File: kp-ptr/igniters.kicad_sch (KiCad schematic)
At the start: 40 parts

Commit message: Footprints IN IMU9DOF OUT Signed-off-by: kretu <krecik@gmail.com>
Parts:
- C39, C40, C41, C42: renamed from C?; footprint (none) -> Capacitor_SMD:C_01005_0402Metric_Pad0.57x0.30mm_HandSolder
- F1, F2, F3, F4: renamed from F?; footprint (none) -> Fuse:Fuse_1206_3216Metric_Pad1.42x1.75mm_HandSolder
- J6, J7, J8, J9: renamed from J?; footprint (none) -> TerminalBlock_TE-Connectivity:TerminalBlock_TE_282834-2_1x02_P2.54mm_Horizontal
- R41, R42, R43, R44, R45, R46, R47, R48, R49, R50, R51, R52, R53, R54, R55, R56, R57, R58, R59, R60: renamed from R?; footprint (none) -> Resistor_SMD:R_01005_0402Metric_Pad0.57x0.30mm_HandSolder
- gave numbers to parts that had none: 8

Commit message: Footprinty drobnicy
Signed-off-by: kretu <krecik@gmail.com>
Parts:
- C39, C40, C41, C42: footprint Capacitor_SMD:C_01005_0402Metric_Pad0.57x0.30mm_HandSolder -> Capacitor_SMD:C_0402_1005Metric_Pad0.74x0.62mm_HandSolder
- R41, R42, R43, R44, R45, R46, R47, R48, R49, R50, R51, R52, R53, R54, R55, R56, R57, R58, R59, R60: footprint Resistor_SMD:R_01005_0402Metric_Pad0.57x0.30mm_HandSolder -> Resistor_SMD:R_0402_1005Metric_Pad0.72x0.64mm_HandSolder
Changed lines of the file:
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@@
     (property "Reference" "R41" (id 0) (at 62.23 100.33 90))
     (property "Value" "10k" (id 1) (at 57.15 100.33 90))
-    (property "Footprint" "Resistor_SMD:R_01005_0402Metric_Pad0.57x0.30mm_HandSolder" (id 2) (at 57.912 99.06 90)
+    (property "Footprint" "Resistor_SMD:R_0402_1005Metric_Pad0.72x0.64mm_HandSolder" (id 2) (at 57.912 99.06 90)
       (effects (font (size 1.27 1.27)) hide)
     )
@@
     (property "Reference" "R52" (id 0) (at 144.78 149.86 90))
     (property "Value" "10k" (id 1) (at 139.7 149.86 90))
-    (property "Footprint" "Resistor_SMD:R_01005_0402Metric_Pad0.57x0.30mm_HandSolder" (id 2) (at 140.462 148.59 90)
+    (property "Footprint" "Resistor_SMD:R_0402_1005Metric_Pad0.72x0.64mm_HandSolder" (id 2) (at 140.462 148.59 90)
       (effects (font (size 1.27 1.27)) hide)
     )
@@
     (property "Reference" "R58" (id 0) (at 151.13 121.92 90))
     (property "Value" "10k" (id 1) (at 151.13 116.84 90))
-    (property "Footprint" "Resistor_SMD:R_01005_0402Metric_Pad0.57x0.30mm_HandSolder" (id 2) (at 151.892 120.65 90)
+    (property "Footprint" "Resistor_SMD:R_0402_1005Metric_Pad0.72x0.64mm_HandSolder" (id 2) (at 151.892 120.65 90)
       (effects (font (size 1.27 1.27)) hide)
     )
@@
       (effects (font (size 1.27 1.27)) (justify left))
     )
-    (property "Footprint" "Capacitor_SMD:C_01005_0402Metric_Pad0.57x0.30mm_HandSolder" (id 2) (at 158.4452 124.46 0)
+    (property "Footprint" "Capacitor_SMD:C_0402_1005Metric_Pad0.74x0.62mm_HandSolder" (id 2) (at 158.4452 124.46 0)
       (effects (font (size 1.27 1.27)) hide)
     )
@@
     (property "Reference" "R54" (id 0) (at 148.59 134.62 90))
     (property "Value" "10k" (id 1) (at 143.51 134.62 90))
-    (property "Footprint" "Resistor_SMD:R_01005_0402Metric_Pad0.57x0.30mm_HandSolder" (id 2) (at 144.272 133.35 90)
+    (property "Footprint" "Resistor_SMD:R_0402_1005Metric_Pad0.72x0.64mm_HandSolder" (id 2) (at 144.272 133.35 90)
       (effects (font (size 1.27 1.27)) hide)
     )
@@
     (property "Reference" "R60" (id 0) (at 189.23 127 90))
     (property "Value" "10k" (id 1) (at 189.23 121.92 90))
-    (property "Footprint" "Resistor_SMD:R_01005_0402Metric_Pad0.57x0.30mm_HandSolder" (id 2) (at 189.992 125.73 90)
+    (property "Footprint" "Resistor_SMD:R_0402_1005Metric_Pad0.72x0.64mm_HandSolder" (id 2) (at 189.992 125.73 90)
       (effects (font (size 1.27 1.27)) hide)
     )
@@
     (property "Reference" "R46" (id 0) (at 67.31 143.51 90))
     (property "Value" "100k" (id 1) (at 67.31 148.59 90))
-    (property "Footprint" "Resistor_SMD:R_01005_0402Metric_Pad0.57x0.30mm_HandSolder" (id 2) (at 66.04 147.828 90)
+    (property "Footprint" "Resistor_SMD:R_0402_1005Metric_Pad0.72x0.64mm_HandSolder" (id 2) (at 66.04 147.828 90)
       (effects (font (size 1.27 1.27)) hide)
     )
@@
     (property "Reference" "R57" (id 0) (at 151.13 72.39 90))
     (property "Value" "10k" (id 1) (at 151.13 67.31 90))
-    (property "Footprint" "Resistor_SMD:R_01005_0402Metric_Pad0.57x0.30mm_HandSolder" (id 2) (at 151.892 71.12 90)
+    (property "Footprint" "Resistor_SMD:R_0402_1005Metric_Pad0.72x0.64mm_HandSolder" (id 2) (at 151.892 71.12 90)
       (effects (font (size 1.27 1.27)) hide)
     )
@@
     (property "Reference" "R47" (id 0) (at 68.58 72.39 90))
     (property "Value" "10k" (id 1) (at 68.58 67.31 90))
-    (property "Footprint" "Resistor_SMD:R_01005_0402Metric_Pad0.57x0.30mm_HandSolder" (id 2) (at 69.342 71.12 90)
+    (property "Footprint" "Resistor_SMD:R_0402_1005Metric_Pad0.72x0.64mm_HandSolder" (id 2) (at 69.342 71.12 90)
       (effects (font (size 1.27 1.27)) hide)
     )
@@
     (property "Reference" "R50" (id 0) (at 106.68 128.27 90))
     (property "Value" "10k" (id 1) (at 106.68 123.19 90))
-    (property "Footprint" "Resistor_SMD:R_01005_0402Metric_Pad0.57x0.30mm_HandSolder" (id 2) (at 107.442 127 90)
+    (property "Footprint" "Resistor_SMD:R_0402_1005Metric_Pad0.72x0.64mm_HandSolder" (id 2) (at 107.442 127 90)
       (effects (font (size 1.27 1.27)) hide)
     )
@@
     (property "Reference" "R42" (id 0) (at 62.23 151.13 90))
     (property "Value" "10k" (id 1) (at 57.15 151.13 90))
-    (property "Footprint" "Resistor_SMD:R_01005_0402Metric_Pad0.57x0.30mm_HandSolder" (id 2) (at 57.912 149.86 90)
+    (property "Footprint" "Resistor_SMD:R_0402_1005Metric_Pad0.72x0.64mm_HandSolder" (id 2) (at 57.912 149.86 90)
       (effects (font (size 1.27 1.27)) hide)
     )
@@
     (property "Reference" "R59" (id 0) (at 189.23 77.47 90))
     (property "Value" "10k" (id 1) (at 189.23 72.39 90))
-    (property "Footprint" "Resistor_SMD:R_01005_0402Metric_Pad0.57x0.30mm_HandSolder" (id 2) (at 189.992 76.2 90)
+    (property "Footprint" "Resistor_SMD:R_0402_1005Metric_Pad0.72x0.64mm_HandSolder" (id 2) (at 189.992 76.2 90)
       (effects (font (size 1.27 1.27)) hide)
     )
@@
       (effects (font (size 1.27 1.27)) (justify left))
     )
-    (property "Footprint" "Capacitor_SMD:C_01005_0402Metric_Pad0.57x0.30mm_HandSolder" (id 2) (at 158.4452 74.93 0)
+    (property "Footprint" "Capacitor_SMD:C_0402_1005Metric_Pad0.74x0.62mm_HandSolder" (id 2) (at 158.4452 74.93 0)
       (effects (font (size 1.27 1.27)) hide)
     )
@@
     (property "Reference" "R51" (id 0) (at 144.78 100.33 90))
     (property "Value" "10k" (id 1) (at 139.7 100.33 90))
-    (property "Footprint" "Resistor_SMD:R_01005_0402Metric_Pad0.57x0.30mm_HandSolder" (id 2) (at 140.462 99.06 90)
+    (property "Footprint" "Resistor_SMD:R_0402_1005Metric_Pad0.72x0.64mm_HandSolder" (id 2) (at 140.462 99.06 90)
       (effects (font (size 1.27 1.27)) hide)
     )
@@
       (effects (font (size 1.27 1.27)) (justify left))
     )
-    (property "Footprint" "Capacitor_SMD:C_01005_0402Metric_Pad0.57x0.30mm_HandSolder" (id 2) (at 75.8952 74.93 0)
+    (property "Footprint" "Capacitor_SMD:C_0402_1005Metric_Pad0.74x0.62mm_HandSolder" (id 2) (at 75.8952 74.93 0)
       (effects (font (size 1.27 1.27)) hide)
     )
@@
     (property "Reference" "R48" (id 0) (at 68.58 123.19 90))
     (property "Value" "10k" (id 1) (at 68.58 118.11 90))
-    (property "Footprint" "Resistor_SMD:R_01005_0402Metric_Pad0.57x0.30mm_HandSolder" (id 2) (at 69.342 121.92 90)
+    (property "Footprint" "Resistor_SMD:R_0402_1005Metric_Pad0.72x0.64mm_HandSolder" (id 2) (at 69.342 121.92 90)
       (effects (font (size 1.27 1.27)) hide)
     )
@@
     (property "Reference" "R43" (id 0) (at 66.04 85.09 90))
     (property "Value" "10k" (id 1) (at 60.96 85.09 90))
-    (property "Footprint" "Resistor_SMD:R_01005_0402Metric_Pad0.57x0.30mm_HandSolder" (id 2) (at 61.722 83.82 90)
+    (property "Footprint" "Resistor_SMD:R_0402_1005Metric_Pad0.72x0.64mm_HandSolder" (id 2) (at 61.722 83.82 90)
       (effects (font (size 1.27 1.27)) hide)
     )
@@
     (property "Reference" "R55" (id 0) (at 149.86 92.71 90))
     (property "Value" "100k" (id 1) (at 149.86 97.79 90))
-    (property "Footprint" "Resistor_SMD:R_01005_0402Metric_Pad0.57x0.30mm_HandSolder" (id 2) (at 148.59 97.028 90)
+    (property "Footprint" "Resistor_SMD:R_0402_1005Metric_Pad0.72x0.64mm_HandSolder" (id 2) (at 148.59 97.028 90)
       (effects (font (size 1.27 1.27)) hide)
     )
@@
     (property "Reference" "R44" (id 0) (at 66.04 135.89 90))
     (property "Value" "10k" (id 1) (at 60.96 135.89 90))
-    (property "Footprint" "Resistor_SMD:R_01005_0402Metric_Pad0.57x0.30mm_HandSolder" (id 2) (at 61.722 134.62 90)
+    (property "Footprint" "Resistor_SMD:R_0402_1005Metric_Pad0.72x0.64mm_HandSolder" (id 2) (at 61.722 134.62 90)
       (effects (font (size 1.27 1.27)) hide)
     )
@@
       (effects (font (size 1.27 1.27)) (justify left))
     )
-    (property "Footprint" "Capacitor_SMD:C_01005_0402Metric_Pad0.57x0.30mm_HandSolder" (id 2) (at 75.8952 125.73 0)
+    (property "Footprint" "Capacitor_SMD:C_0402_1005Metric_Pad0.74x0.62mm_HandSolder" (id 2) (at 75.8952 125.73 0)
       (effects (font (size 1.27 1.27)) hide)
     )
@@
     (property "Reference" "R45" (id 0) (at 67.31 92.71 90))
     (property "Value" "100k" (id 1) (at 67.31 97.79 90))
-    (property "Footprint" "Resistor_SMD:R_01005_0402Metric_Pad0.57x0.30mm_HandSolder" (id 2) (at 66.04 97.028 90)
+    (property "Footprint" "Resistor_SMD:R_0402_1005Metric_Pad0.72x0.64mm_HandSolder" (id 2) (at 66.04 97.028 90)
       (effects (font (size 1.27 1.27)) hide)
     )
@@
     (property "Reference" "R56" (id 0) (at 149.86 142.24 90))
     (property "Value" "100k" (id 1) (at 149.86 147.32 90))
-    (property "Footprint" "Resistor_SMD:R_01005_0402Metric_Pad0.57x0.30mm_HandSolder" (id 2) (at 148.59 146.558 90)
+    (property "Footprint" "Resistor_SMD:R_0402_1005Metric_Pad0.72x0.64mm_HandSolder" (id 2) (at 148.59 146.558 90)
       (effects (font (size 1.27 1.27)) hide)
     )
@@
     (property "Reference" "R53" (id 0) (at 148.59 85.09 90))
     (property "Value" "10k" (id 1) (at 143.51 85.09 90))
-    (property "Footprint" "Resistor_SMD:R_01005_0402Metric_Pad0.57x0.30mm_HandSolder" (id 2) (at 144.272 83.82 90)
+    (property "Footprint" "Resistor_SMD:R_0402_1005Metric_Pad0.72x0.64mm_HandSolder" (id 2) (at 144.272 83.82 90)
       (effects (font (size 1.27 1.27)) hide)
     )
@@
     (property "Reference" "R49" (id 0) (at 106.68 77.47 90))
     (property "Value" "10k" (id 1) (at 106.68 72.39 90))
-    (property "Footprint" "Resistor_SMD:R_01005_0402Metric_Pad0.57x0.30mm_HandSolder" (id 2) (at 107.442 76.2 90)
-      (effects (font (size 1.27 1.27)) hide)
-    )
+    (property "Footprint" "Resistor_SMD:R_0402_1005Metric_Pad0.72x0.64mm_HandSolder" (id 2) (at 107.442 76.2 90)
+      (effects (font (size 1.27 1.27)) hide)
+    )

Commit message: Kilka zmian.
-dodany tranzystor P/N mosfet do biblioteki i zapalników
-dodany komentarz o impedancji ścieżek RF
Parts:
- removed Q10, Q11, Q6, Q7: NMOS_SOT23, Package_TO_SOT_SMD:SOT-23, symbol Transistor_FET:IRLML2060
- removed Q12, Q13, Q8, Q9: PMOS_SOT23, Package_TO_SOT_SMD:SOT-23, symbol Transistor_FET:IRLML6401
- added Q? (x8): DMC2025UFDB, symbol KP-PTR_lib:DMC2025UFDB
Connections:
- net Earth: now also Q?.S1, Q?.S1, Q?.S1, Q?.S1
- net IGN1_EN: now also Q?.G1 (G2)
- net IGN2_EN: now also Q?.G1 (G2)
- net IGN3_EN: now also Q?.G1 (G2)
- net IGN4_EN: now also Q?.G1 (G2)
- net at C41.2, R57.2: now also Q?.D1 (D2), Q?.G2
- net at C41.1, F3.2, R57.1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: now also Q?.S2
- net at J8.1 (Pin_1), R55.2, R59.2: now also Q?.D2
- net at C39.2, R47.2: now also Q?.D1 (D2), Q?.G2
- net at C39.1, F1.2, R47.1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: now also Q?.S2
- net at J6.1 (Pin_1), R45.2, R49.2: now also Q?.D2
- net at C42.2, R58.2: now also Q?.D1 (D2), Q?.G2
- net at J9.1 (Pin_1), R56.2, R60.2: now also Q?.D2
- net at C42.1, F4.2, R58.1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: now also Q?.S2
- net at J7.1 (Pin_1), R46.2, R50.2: now also Q?.D2
- net at C40.1, F2.2, R48.1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: now also Q?.S2
- net at C40.2, R48.2: now also Q?.D1 (D2), Q?.G2
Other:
- note removed: "Do dopracowania: -estetyka -zweryfikować z poprzednimi projektami"

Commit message: Update po spotkaniu
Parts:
- C39, C40, C41, C42: footprint Capacitor_SMD:C_0402_1005Metric_Pad0.74x0.62mm_HandSolder -> Capacitor_SMD:C_0402_1005Metric
- F1, F2, F3, F4: footprint Fuse:Fuse_1206_3216Metric_Pad1.42x1.75mm_HandSolder -> Fuse:Fuse_0805_2012Metric
- R41, R42, R43, R44, R45, R46, R47, R48, R49, R50, R51, R52, R53, R54, R55, R56, R57, R58, R59, R60: footprint Resistor_SMD:R_0402_1005Metric_Pad0.72x0.64mm_HandSolder -> Resistor_SMD:R_0402_1005Metric
- gave numbers to parts that had none: 4

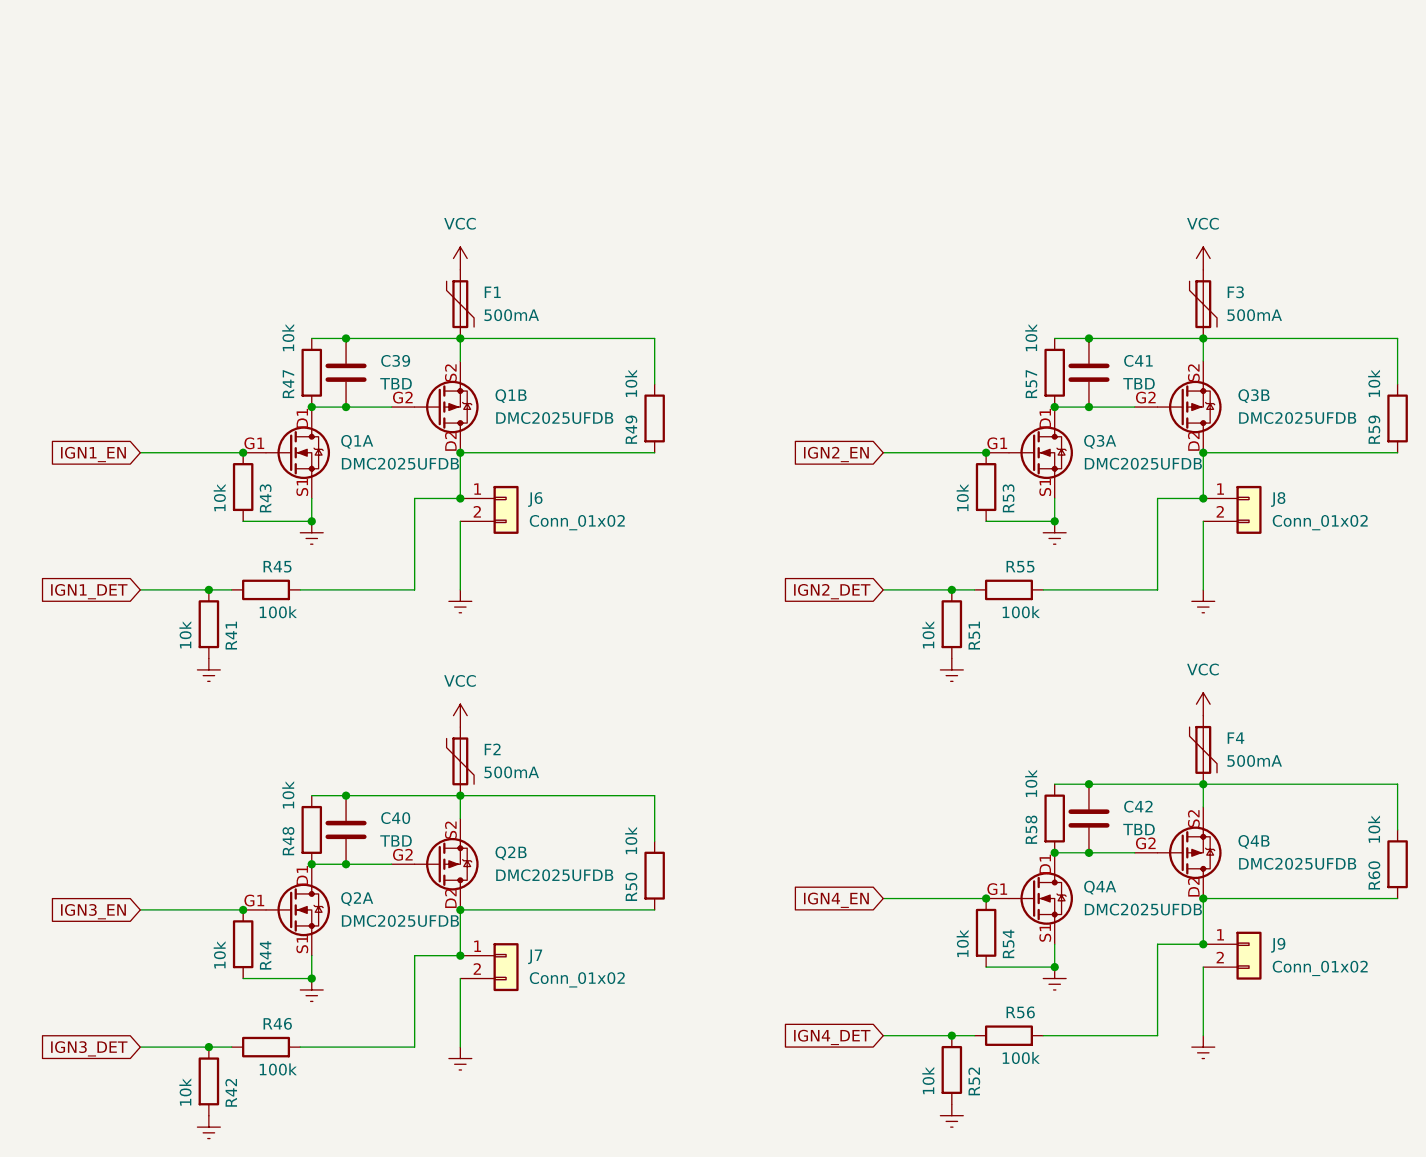
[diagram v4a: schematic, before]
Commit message: Footprint mosfeta
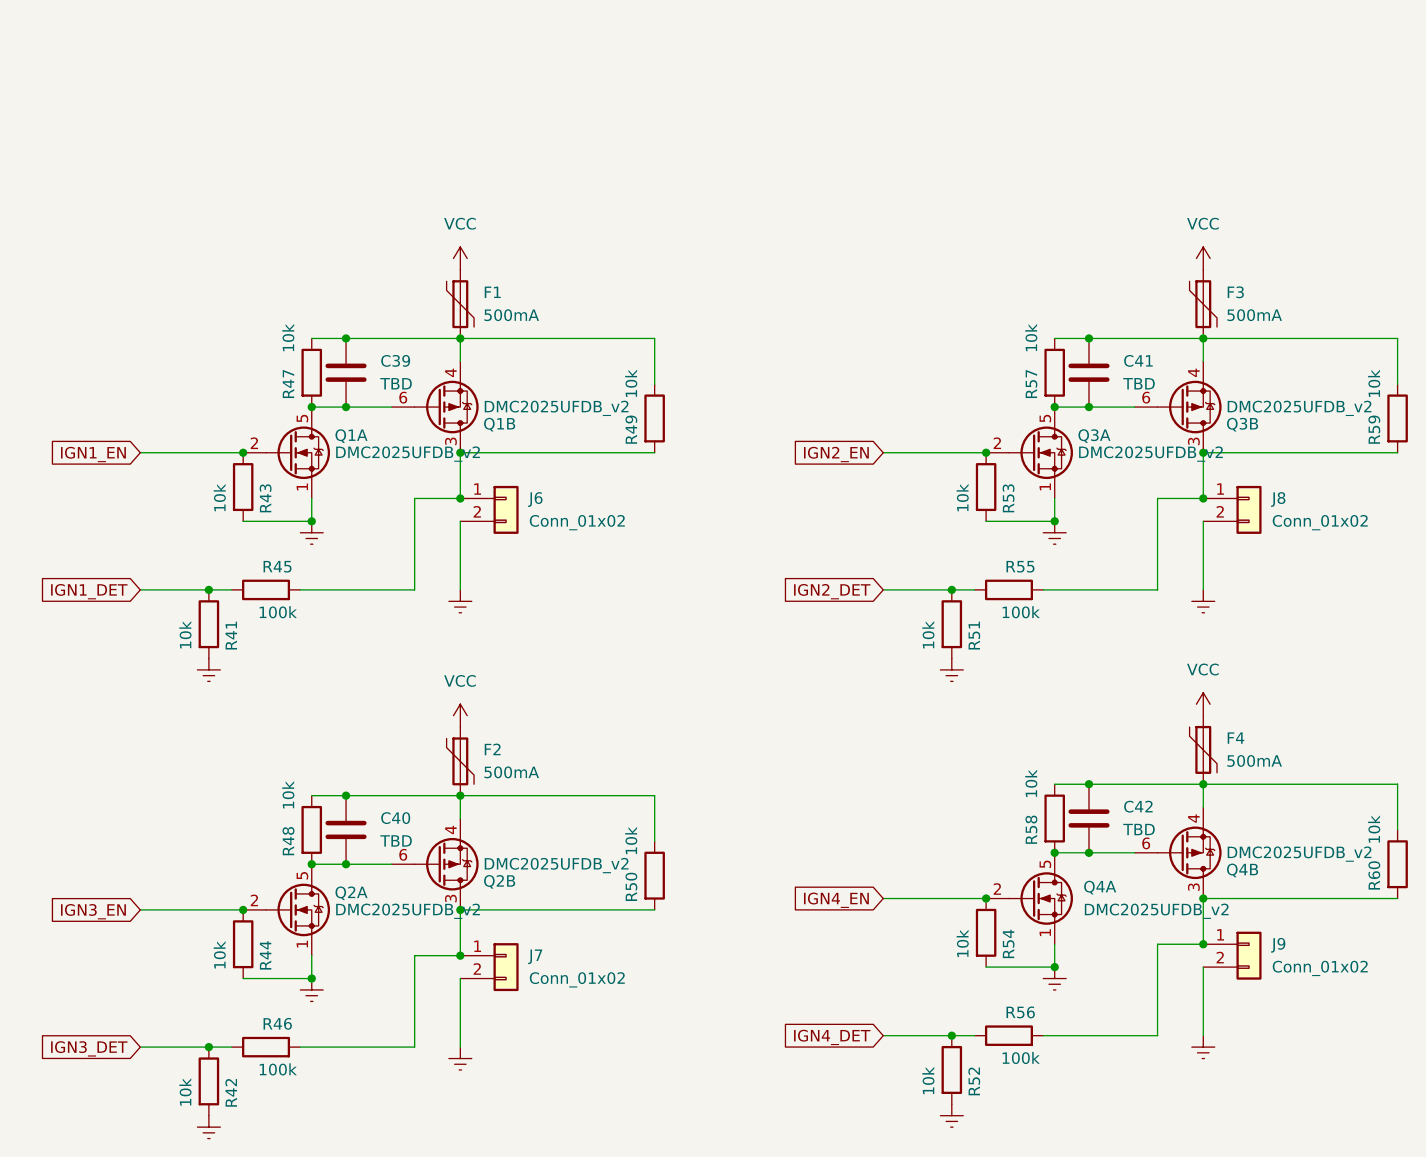
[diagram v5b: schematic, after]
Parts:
- J9: footprint TerminalBlock_TE-Connectivity:TerminalBlock_TE_282834-2_1x02_P2.54mm_Horizontal -> TerminalBlock_Phoenix:TerminalBlock_Phoenix_MPT-0,5-2-2.54_1x02_P2.54mm_Horizontal
- Q1, Q2, Q3, Q4: value DMC2025UFDB -> DMC2025UFDB_v2; footprint (none) -> KP-PTR_lib:DMC2025UFDB; symbol KP-PTR_lib:DMC2025UFDB -> KP-PTR_lib:DMC2025UFDB_v2
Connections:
- net Earth: now also Q1.1 (S1), Q2.1 (S1), Q3.1 (S1), Q4.1 (S1); no longer Q1.S1, Q2.S1, Q3.S1, Q4.S1
- net IGN1_EN: now also Q1.2 (G1); no longer Q1.G1 (G2)
- net IGN2_EN: now also Q3.2 (G1); no longer Q3.G1 (G2)
- net IGN3_EN: now also Q2.2 (G1); no longer Q2.G1 (G2)
- net IGN4_EN: now also Q4.2 (G1); no longer Q4.G1 (G2)
- net at J7.1 (Pin_1), R46.2, R50.2: now also Q2.3 (D2); no longer Q2.D2
- net at C40.2, R48.2: now also Q2.5 (D1), Q2.6 (G2); no longer Q2.D1 (D2), Q2.G2
- net at C40.1, F2.2, R48.1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: now also Q2.4 (S2); no longer Q2.S2
- net at J9.1 (Pin_1), R56.2, R60.2: now also Q4.3 (D2); no longer Q4.D2
- net at C42.2, R58.2: now also Q4.5 (D1), Q4.6 (G2); no longer Q4.D1 (D2), Q4.G2
- net at C42.1, F4.2, R58.1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: now also Q4.4 (S2); no longer Q4.S2
- net at J6.1 (Pin_1), R45.2, R49.2: now also Q1.3 (D2); no longer Q1.D2
- net at C39.2, R47.2: now also Q1.5 (D1), Q1.6 (G2); no longer Q1.D1 (D2), Q1.G2
- net at C39.1, F1.2, R47.1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: now also Q1.4 (S2); no longer Q1.S2
- net at C41.1, F3.2, R57.1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: now also Q3.4 (S2); no longer Q3.S2
- net at C41.2, R57.2: now also Q3.5 (D1), Q3.6 (G2); no longer Q3.D1 (D2), Q3.G2
- net at J8.1 (Pin_1), R55.2, R59.2: now also Q3.3 (D2); no longer Q3.D2

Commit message: Grupowanie
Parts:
- J10: renamed from J6; footprint TerminalBlock_TE-Connectivity:TerminalBlock_TE_282834-2_1x02_P2.54mm_Horizontal -> TerminalBlock_Phoenix:TerminalBlock_Phoenix_MPT-0,5-2-2.54_1x02_P2.54mm_Horizontal
- J11: renamed from J7; footprint TerminalBlock_TE-Connectivity:TerminalBlock_TE_282834-2_1x02_P2.54mm_Horizontal -> TerminalBlock_Phoenix:TerminalBlock_Phoenix_MPT-0,5-2-2.54_1x02_P2.54mm_Horizontal
- J12: renamed from J8; footprint TerminalBlock_TE-Connectivity:TerminalBlock_TE_282834-2_1x02_P2.54mm_Horizontal -> TerminalBlock_Phoenix:TerminalBlock_Phoenix_MPT-0,5-2-2.54_1x02_P2.54mm_Horizontal
- renumbered C39 to C47, C40 to C48, C41 to C49, C42 to C50, F1 to F2, F2 to F3, F3 to F4, F4 to F5, J9 to J13, Q1 to Q2, Q2 to Q3, Q3 to Q4, Q4 to Q5, R41 to R44, R42 to R45, R43 to R46, R44 to R47, R45 to R48, R46 to R49, R47 to R50, R48 to R51, R49 to R52, R50 to R53, R51 to R54, R52 to R55, R53 to R56, R54 to R57, R55 to R58, R56 to R59, R57 to R60, R58 to R61, R59 to R62, R60 to R63
